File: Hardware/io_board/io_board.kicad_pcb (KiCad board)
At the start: 2 copper layers, 80.8 x 60.1 mm, 33 parts, among them J1 Conn_01x40, J2 Conn_02x05_Odd_Even, J3 Mini-DIN-6, J4 Conn_02x10_Odd_Even, U1 74LS137, U2 W65C22NxP

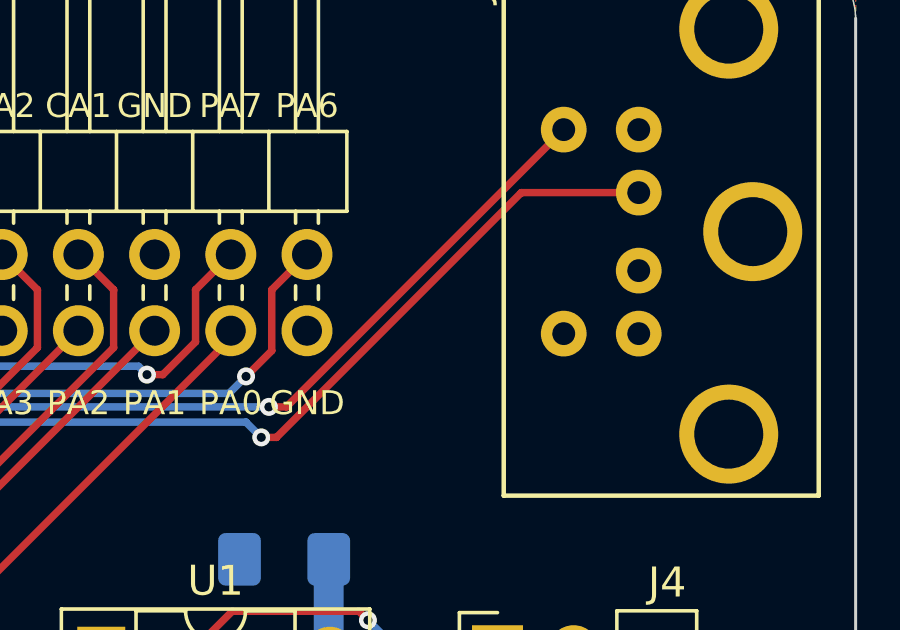
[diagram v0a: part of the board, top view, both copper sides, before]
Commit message: Many updates. SLOW signal is now shared amongst all slots, so their output has to be open drain.
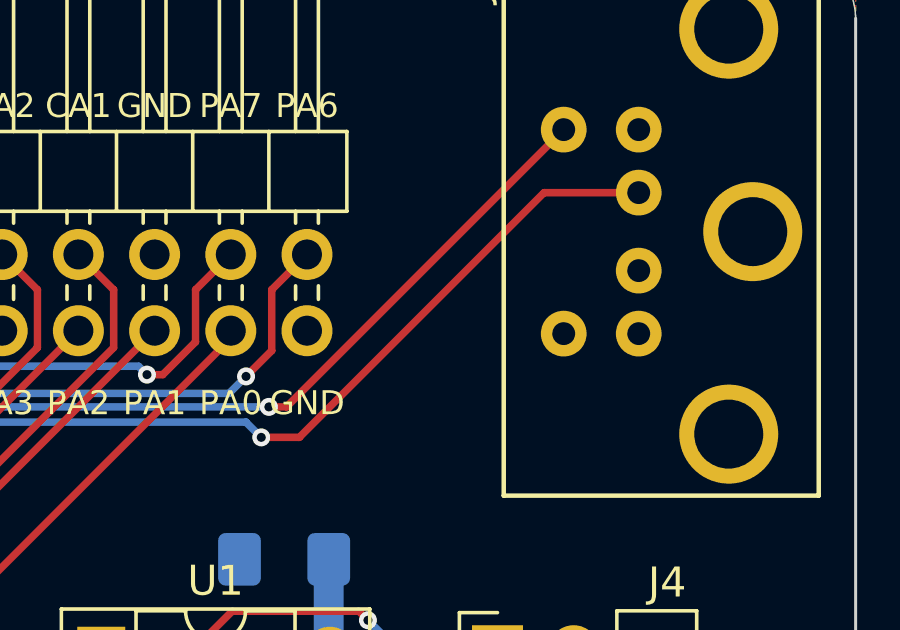
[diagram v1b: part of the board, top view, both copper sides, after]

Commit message: redo gerbers before ordering prototype boards
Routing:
- net ~RESET~: track 29.1 -> 31.3 mm
- net LED4: track 85.5 -> 84.0 mm
- net LED1: track 64.8 -> 66.2 mm
- net Net-(J3-Pad5): track 76.8 -> 77.9 mm
- net LED3: track 67.9 -> 67.3 mm

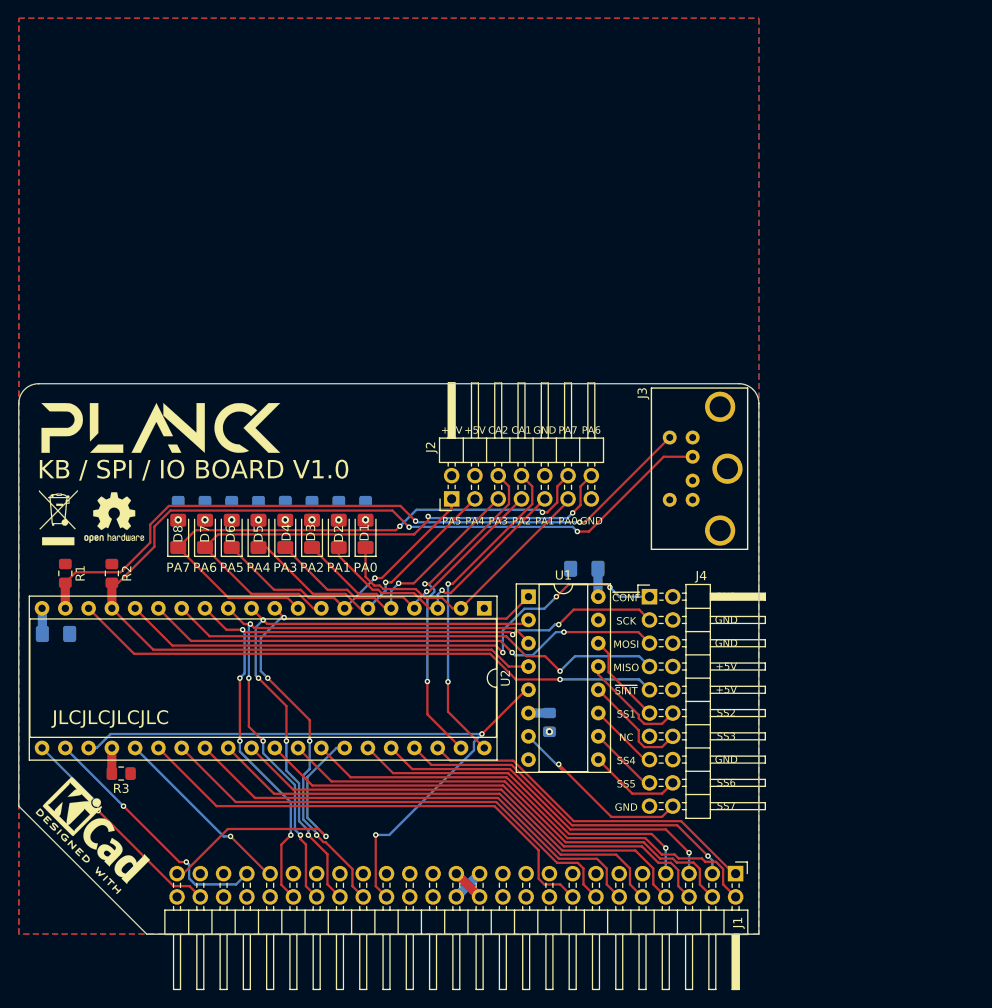
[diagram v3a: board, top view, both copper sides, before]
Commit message: [WIP] add 74HS14 schmitt trigger inverter to PS/2 data and clock signals
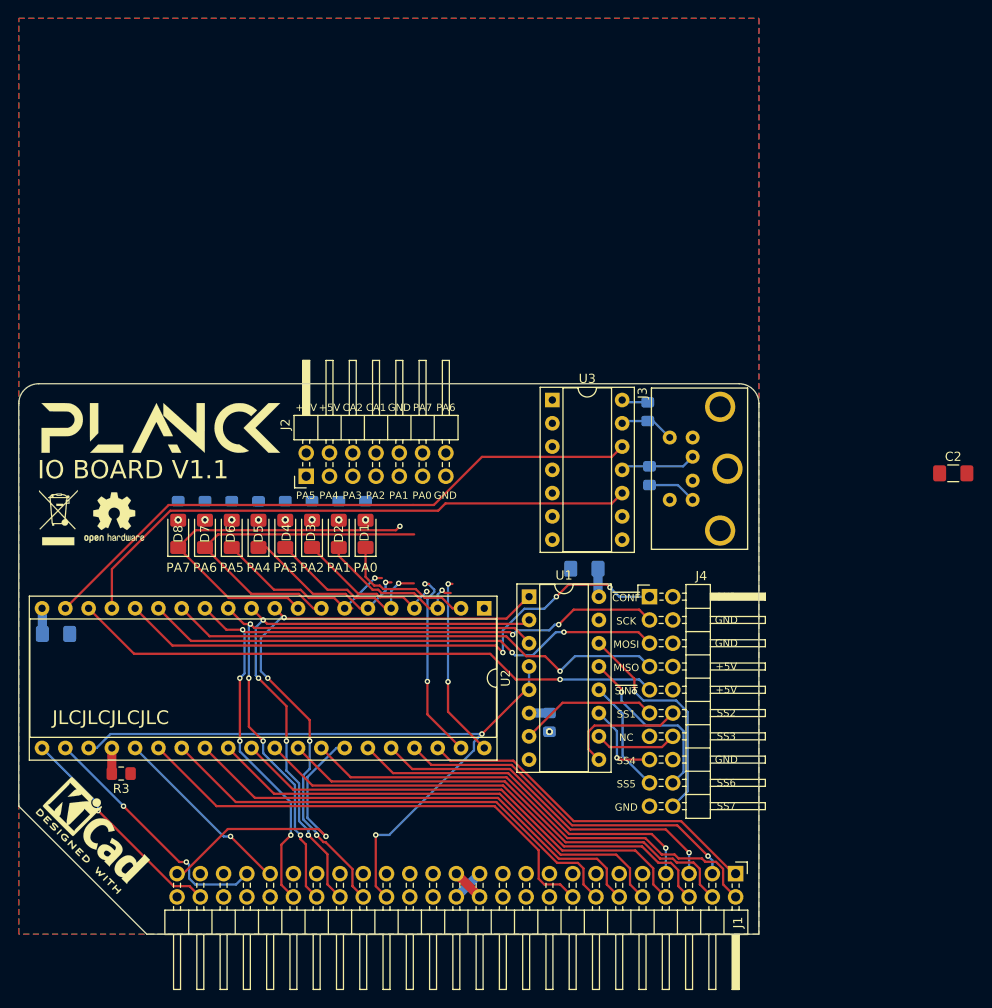
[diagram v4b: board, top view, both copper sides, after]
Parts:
- added C2: C_Small, Capacitor_SMD:C_1206_3216Metric_Pad1.42x1.75mm_HandSolder, F.Cu at (102.0, -50.3)
- added U3: 74LS14, Package_DIP:DIP-14_W7.62mm_Socket, F.Cu at (58.2, -58.3)
- R1, R2: moved to B.Cu
- U1: value 74LS137 -> 74LS138
- moved R1 66.0 mm to (68.6, -57.0)
- moved R2 59.6 mm to (68.8, -50.0), turned to 90 degrees
- moved J2 16.1 mm to (31.4, -50.0)
- moved U1 0.06 mm to (55.7, -36.8)
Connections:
- J1 pad 22: EX2 -> ~SLOW~
- J1 pad 42: EX3 -> CLK_12M
- J1 pad 44: EX4 -> EX2
- J1 pad 46: EX5 -> EX3
- U1 pad 10: /SS5 -> /SS3
- U1 pad 12: /SS3 -> /SS5
- U1 pad 13: /SS2 -> /SS6
- U1 pad 14: /SS1 -> /SS7
- U1 pad 4: PS2_DATA -> ~SLOT_SEL~
- U1 pad 7: /SS7 -> /SS1
- U1 pad 9: /SS6 -> /SS2
- U2 pad 17: PS2_DATA -> Net-(U2-Pad17)
- U2 pad 19: Net-(J3-Pad5) -> Net-(U2-Pad19)
- U2 pad 25: CLK -> CLK_12M
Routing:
- net PS2_DATA: track 123.2 -> 8.28 mm, vias 2 -> 0
- net Net-(J3-Pad5): track 77.9 -> 6.04 mm, vias 2 -> 0
- net Net-(U2-Pad19): track 0.00 -> 68.1 mm
- net Net-(U2-Pad17): track 0.00 -> 63.4 mm
- net /PA6: track 62.4 -> 38.9 mm, vias 2 -> 0
- net /PA7: track 62.9 -> 41.0 mm, vias 2 -> 1
- net /PA0: track 32.5 -> 15.7 mm
- net /CA2: track 36.8 -> 20.9 mm
- net /CA1: track 35.9 -> 20.0 mm
- net /PA1: track 32.1 -> 17.6 mm
- net /PA2: track 31.1 -> 16.8 mm
- net /PA3: track 32.3 -> 19.3 mm
- net /PA5: track 34.3 -> 21.4 mm
- net /PA4: track 32.1 -> 19.2 mm
- net /SS6: track 10.2 -> 19.1 mm, vias 0 -> 1
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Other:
- board text added: "IO BOARD V1.1"

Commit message: small fixes on the hardware
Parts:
- added C3: C_Small, Capacitor_SMD:C_1206_3216Metric_Pad1.42x1.75mm_HandSolder, B.Cu at (63.2, -56.8)
- C2: moved to B.Cu
- moved C2 30.5 mm to (71.9, -44.8), turned to 180 degrees
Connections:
- C2 pad 2: GND -> Net-(C2-Pad2)
- U3 pad 1: GND -> Net-(J3-Pad5)
- U3 pad 11: PS2_DATA -> Net-(U3-Pad11)
- U3 pad 12: Net-(U2-Pad19) -> Net-(U3-Pad11)
- U3 pad 13: Net-(J3-Pad5) -> PS2_DATA
- U3 pad 3: GND -> Net-(U3-Pad2)
- U3 pad 4: Net-(U3-Pad4) -> Net-(U2-Pad19)
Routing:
- net /CA1: track 20.0 -> 38.3 mm, vias 2 -> 3
- net /CA2: track 20.9 -> 38.6 mm, vias 2 -> 3
- net /PA0: track 15.7 -> 26.5 mm
- net /PA2: track 16.8 -> 26.0 mm, vias 1 -> 0
- net Net-(J3-Pad5): track 6.04 -> 14.5 mm
- net /PA6: track 38.9 -> 47.2 mm
- net /PA7: track 41.0 -> 48.9 mm, vias 1 -> 0
- net /PA4: track 19.2 -> 27.1 mm, vias 1 -> 0
- net /PA1: track 17.6 -> 25.3 mm, vias 1 -> 0
- net /PA3: track 19.3 -> 26.3 mm, vias 1 -> 0
- net /PA5: track 21.4 -> 27.7 mm, vias 1 -> 0
- net Net-(U2-Pad17): track 63.4 -> 69.3 mm
- net +5V: track 17.7 -> 23.0 mm
- net Net-(U2-Pad19): track 68.1 -> 63.5 mm
- net PS2_DATA: track 8.28 -> 11.4 mm
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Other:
- board text added: "KB / SPI / IO BOARD V1.1"
- board text removed: "KB / SPI / IO BOARD V1.0"
